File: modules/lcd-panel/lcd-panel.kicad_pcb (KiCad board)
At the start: 2 copper layers, 3 parts, among them J1 5051100692, J2 5051104091, U1 LP8556SQ-E09/NOPB

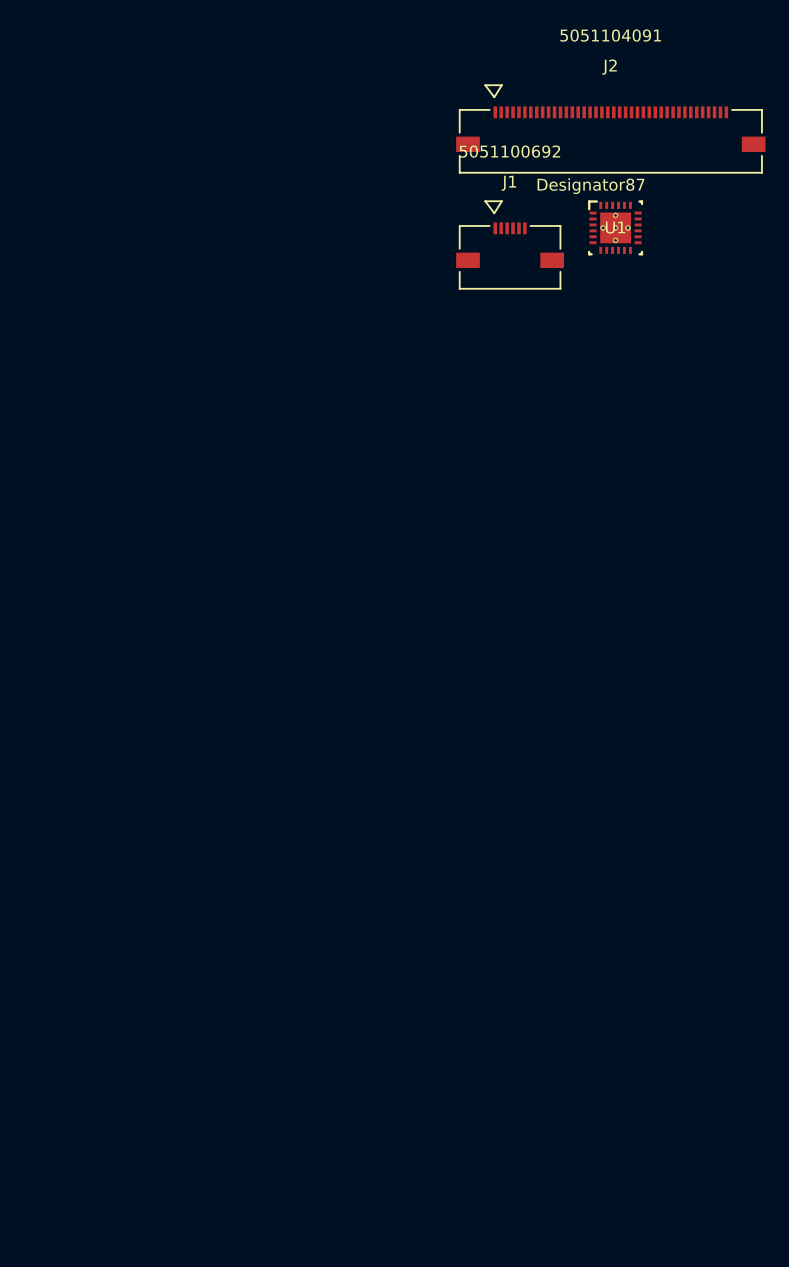
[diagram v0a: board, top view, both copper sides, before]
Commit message: Finish LCD - updating projects
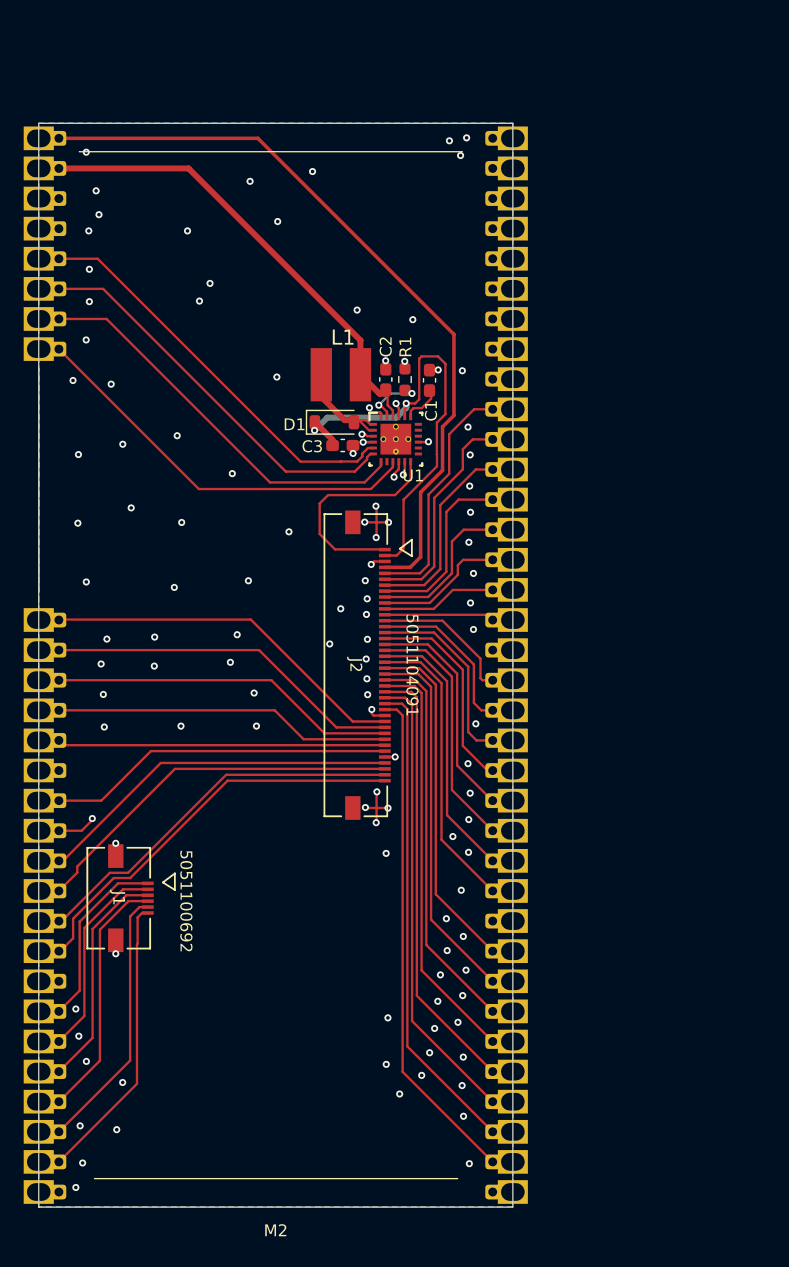
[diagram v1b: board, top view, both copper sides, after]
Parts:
- added C1: 10uF, Capacitor_SMD:C_0603_1608Metric_Pad1.08x0.95mm_HandSolder, F.Cu at (121.4, 71.9)
- added C2: 2.2uF, Capacitor_SMD:C_0603_1608Metric_Pad1.08x0.95mm_HandSolder, F.Cu at (117.7, 71.8)
- added C3: 4.7uF, Capacitor_SMD:C_0603_1608Metric_Pad1.08x0.95mm_HandSolder, F.Cu at (114.0, 77.4)
- added D1: STPS340U, Diode_SMD:D_SOD-123, F.Cu at (113.3, 75.4)
- added L1: SDR0403-4R7ML, lcd-panel:SDR0403, F.Cu at (113.9, 71.4)
- added M2: ~, MegaCastle:MegaCastle2x36-Module-I40.0x86.6-MFFFFFFFFFFFFFF-SPAREPAD, F.Cu at (108.4, 95.9)
- added R1: 30K, Resistor_SMD:R_0603_1608Metric_Pad0.98x0.95mm_HandSolder, F.Cu at (119.3, 71.8)
- moved J1 63.4 mm to (95.1, 115.5), turned to -90 degrees
- moved J2 49.2 mm to (115.2, 95.9), turned to -90 degrees
- moved U1 25.7 mm to (118.5, 76.8)
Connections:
- net Net-(D1-A) renamed /SW
- J1 pad 1: CTP_PIN1 -> CPT_SCL
- J1 pad 2: CTP_PIN2 -> CPT_SDA
- J1 pad 3: CTP_PIN3 -> CPT_VDD
- J1 pad 4: CTP_PIN4 -> CPT_WAKE
- J1 pad 5: CTP_PIN5 -> CTP_INT
- J1 pad 6: CTP_PIN6 -> CTP_GND
- U1 pad 19: Net-(U1-VLDO) -> /VLDO
- U1 pad 23: Net-(U1-ISET) -> /ISET
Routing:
- net LCD_3V3: track 0.00 -> 63.5 mm
- net BLUE7: track 0.00 -> 42.5 mm
- net BLUE6: track 0.00 -> 40.7 mm
- net VBAT: track 0.00 -> 40.1 mm
- net LEDA: track 0.00 -> 39.5 mm, vias 0 -> 2
- net BLUE5: track 0.00 -> 38.9 mm
- net BLUE4: track 0.00 -> 37.1 mm
- net BLUE3: track 0.00 -> 35.2 mm
- net RESIST_YU: track 0.00 -> 34.4 mm
- net BL_PWM: track 0.00 -> 34.3 mm
- net BL_SDA: track 0.00 -> 34.2 mm
- net BL_3V3: track 0.00 -> 33.8 mm
- net BL_SCL: track 0.00 -> 33.6 mm
- net BLUE2: track 0.00 -> 33.2 mm
- net RESIST_XL: track 0.00 -> 32.6 mm
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- added copper zone on B.Cu, net GND
- added copper zone on F.Cu, net GND
- added copper zone on In1.Cu, net GND
- added copper zone on In2.Cu, net GND
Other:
- board outline added: 40 x 91.4 mm
- copper layers 2 -> 4
